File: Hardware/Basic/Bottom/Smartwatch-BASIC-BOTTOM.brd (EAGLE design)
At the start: 33 x 33 mm, 37 parts, among them U1 AD5242-SO16, U3 PCF8523

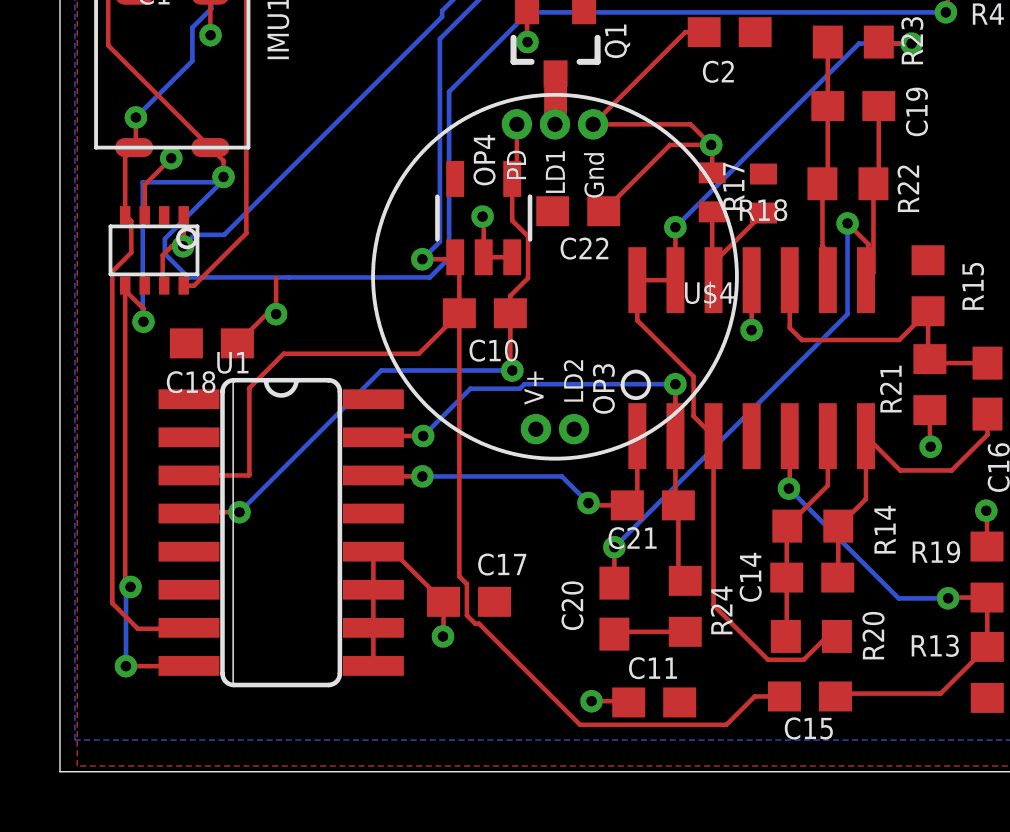
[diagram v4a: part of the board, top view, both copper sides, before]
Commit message: Bottom Board Complete
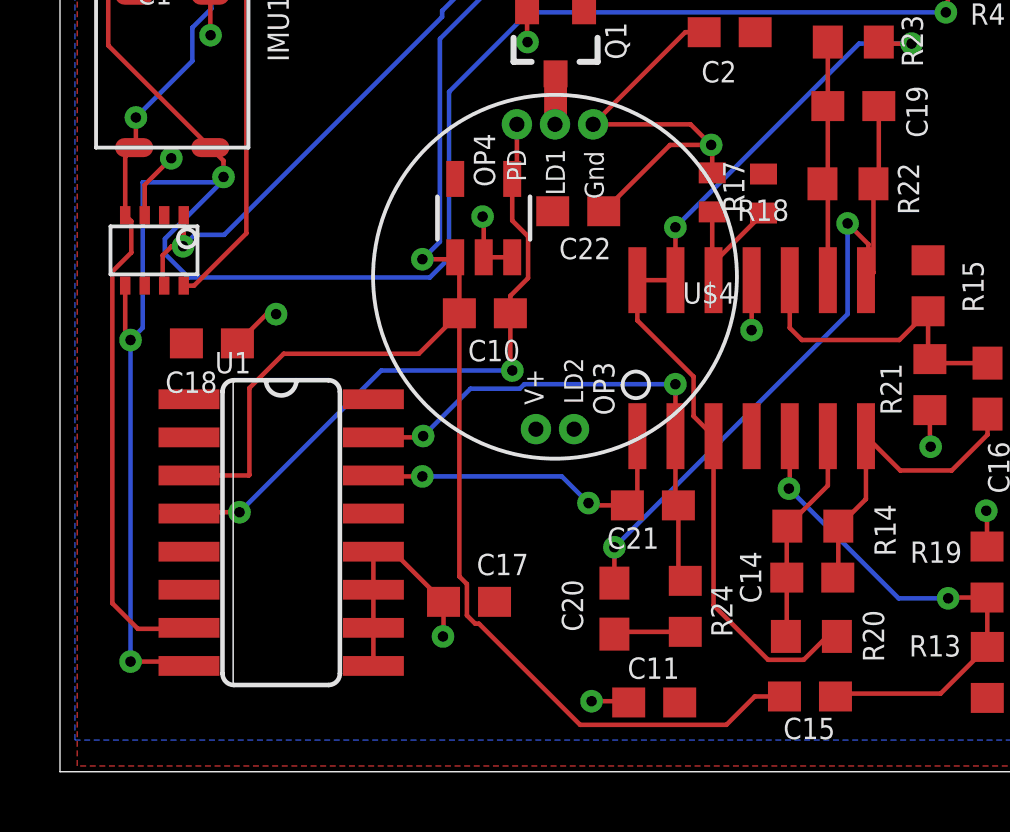
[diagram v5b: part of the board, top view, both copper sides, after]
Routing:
- net GND: track 40.9 -> 39.7 mm
- net SDA: track 76.0 -> 75.0 mm, vias 5 -> 4
- net N$18: track 7.10 -> 8.08 mm
- net G.W2: track 16.7 -> 17.6 mm
- net SCL: track 56.6 -> 57.5 mm
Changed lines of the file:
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@@
 <wire x1="9.3882" y1="17.7546" x2="9.7028" y2="17.7546" width="0.1524" layer="1"/>
 <via x="9.7028" y="17.7546" extent="1-16" drill="0.35"/>
-<wire x1="9.7028" y1="18.962" x2="9.7028" y2="17.7546" width="0.1524" layer="1"/>
 <wire x1="9.7536" y1="17.7038" x2="9.7028" y2="17.7546" width="0.1524" layer="1"/>
 </signal>
@@
 <wire x1="5.4614" y1="29.8034" x2="5.4614" y2="28.8744" width="0.1524" layer="1"/>
 <wire x1="5.4614" y1="28.8744" x2="4.9718" y2="28.3848" width="0.1524" layer="1"/>
-<wire x1="5.3238" y1="18.7024" x2="6.7136" y2="16.78" width="0" layer="19" extent="1-1"/>
 </signal>
 <signal name="SDA">
@@
 <wire x1="31.9096" y1="29.3368" x2="32.0936" y2="29.1528" width="0.1524" layer="1"/>
 <contactref element="J1" pad="1"/>
-<wire x1="4.6738" y1="18.7024" x2="4.6738" y2="8.8392" width="0.1524" layer="1"/>
-<wire x1="4.6738" y1="8.8392" x2="4.8516" y2="8.6614" width="0.1524" layer="1"/>
-<via x="4.8516" y="8.6614" extent="1-16" drill="0.35"/>
-<wire x1="4.8516" y1="8.6614" x2="4.699" y2="8.5088" width="0.1524" layer="16"/>
-<wire x1="4.699" y1="8.5088" x2="4.699" y2="6.0198" width="0.1524" layer="16"/>
-<via x="4.699" y="6.0198" extent="1-16" drill="0.35"/>
-<wire x1="4.699" y1="6.0198" x2="6.793" y2="6.0198" width="0.1524" layer="1"/>
 <wire x1="6.793" y1="6.0198" x2="6.7996" y2="6.0264" width="0.1524" layer="1"/>
 <wire x1="5" y1="33" x2="5" y2="30.7152875" width="0.1524" layer="1"/>
@@
 <wire x1="7.9502" y1="22.3266" x2="7.7724" y2="22.1488" width="0.1524" layer="16"/>
 <wire x1="7.7724" y1="22.1488" x2="5.2578" y2="22.1488" width="0.1524" layer="16"/>
-<wire x1="5.2578" y1="22.1488" x2="5.2578" y2="17.526" width="0.1524" layer="16"/>
-<wire x1="5.2578" y1="17.526" x2="5.2832" y2="17.5006" width="0.1524" layer="16"/>
-<via x="5.2832" y="17.5006" extent="1-16" drill="0.35"/>
-<wire x1="5.2832" y1="17.5006" x2="5.2832" y2="17.9324" width="0.1524" layer="1"/>
-<wire x1="5.2832" y1="17.9447125" x2="5.2832" y2="17.9324" width="0.1524" layer="1"/>
 <wire x1="32.0936" y1="29.1528" x2="32.0936" y2="27.8772" width="0.1524" layer="1"/>
 <wire x1="32.0936" y1="27.8772" x2="32.0294" y2="27.813" width="0.1524" layer="1"/>
@@
 <wire x1="5.9972" y1="20.26655" x2="7.9502" y2="22.21955" width="0.1524" layer="16"/>
 <wire x1="7.9502" y1="22.21955" x2="7.9502" y2="22.3266" width="0.1524" layer="16"/>
-<wire x1="14.83095" y1="18.9766" x2="10.1346" y2="18.9766" width="0.1524" layer="16"/>
-<wire x1="10.1346" y1="18.9766" x2="6.78445" y2="18.9766" width="0.1524" layer="16"/>
+<wire x1="14.83095" y1="18.9766" x2="6.78445" y2="18.9766" width="0.1524" layer="16"/>
 <wire x1="6.78445" y1="18.9766" x2="5.9972" y2="19.76385" width="0.1524" layer="16"/>
 <wire x1="7.5118" y1="23.3048" x2="7.9502" y2="22.8664" width="0.1524" layer="1"/>
 <wire x1="7.9502" y1="22.8664" x2="7.9502" y2="22.3266" width="0.1524" layer="1"/>
-<wire x1="5.2832" y1="17.9324" x2="4.6738" y2="18.5418" width="0.1524" layer="1"/>
-<wire x1="4.6738" y1="18.5418" x2="4.6738" y2="18.7024" width="0.1524" layer="1"/>
+<wire x1="4.6738" y1="17.0688" x2="4.8516" y2="16.891" width="0.1524" layer="1"/>
+<via x="4.8516" y="16.891" extent="1-16" drill="0.35"/>
+<wire x1="5.2578" y1="17.2972" x2="4.8516" y2="16.891" width="0.1524" layer="16"/>
+<wire x1="5.2578" y1="22.1488" x2="5.2578" y2="17.2972" width="0.1524" layer="16"/>
+<wire x1="4.8516" y1="16.891" x2="4.8516" y2="6.1724" width="0.1524" layer="16"/>
+<via x="4.8516" y="6.1724" extent="1-16" drill="0.35"/>
+<wire x1="4.8516" y1="6.1724" x2="6.6404" y2="6.1724" width="0.1524" layer="1"/>
+<wire x1="6.6404" y1="6.1724" x2="6.793" y2="6.0198" width="0.1524" layer="1"/>
+<wire x1="4.6738" y1="18.7024" x2="4.6738" y2="17.0688" width="0.1524" layer="1"/>
 </signal>
 <signal name="SCL">
@@
 <contactref element="J1" pad="2"/>
 <wire x1="4.2448" y1="8.1168875" x2="5.0972875" y2="7.2644" width="0.1524" layer="1"/>
-<wire x1="5.0972875" y1="7.2644" x2="5.969" y2="7.2644" width="0.1524" layer="1"/>
 <wire x1="7.54" y1="33" x2="7.54" y2="31.068" width="0.1524" layer="1"/>
 <wire x1="7.54" y1="31.068" x2="7.5438" y2="31.0642" width="0.1524" layer="1"/>
@@
 <wire x1="32.3088" y1="32.0548" x2="31.8996" y2="31.6456" width="0.1524" layer="16"/>
 <wire x1="31.8996" y1="31.6456" x2="14.91245" y2="31.6456" width="0.1524" layer="16"/>
-<wire x1="5.969" y1="7.2644" x2="6.7996" y2="7.2964" width="0" layer="19" extent="1-1"/>
+<wire x1="5.0972875" y1="7.2644" x2="6.7676" y2="7.2644" width="0.1524" layer="1"/>
+<wire x1="6.7676" y1="7.2644" x2="6.7996" y2="7.2964" width="0.1524" layer="1"/>
 </signal>
 <signal name="A6/TIA">
@@
 <wire x1="16.1826" y1="15.2682" x2="14.605" y2="13.6906" width="0.1524" layer="16"/>
 <wire x1="17.82815" y1="15.2682" x2="16.1826" y2="15.2682" width="0.1524" layer="16"/>
-<wire x1="14.605" y1="13.6906" x2="13.7922" y2="13.6906" width="0.1524" layer="1"/>
 <wire x1="13.7922" y1="13.6906" x2="13.7414" y2="13.6398" width="0.1524" layer="1"/>
-<wire x1="13.7414" y1="13.6398" x2="12.9464" y2="13.6464" width="0" layer="19" extent="1-1"/>
+<wire x1="14.605" y1="13.6906" x2="14.5608" y2="13.6464" width="0.1524" layer="1"/>
+<wire x1="14.5608" y1="13.6464" x2="12.9464" y2="13.6464" width="0.1524" layer="1"/>
+<wire x1="14.605" y1="13.6906" x2="13.7922" y2="13.6906" width="0" layer="19" extent="1-1"/>
 </signal>
 <signal name="G.A1">
@@
 <contactref element="C19" pad="2"/>
 <contactref element="R23" pad="2"/>
-<wire x1="27.9152" y1="22.098" x2="27.9152" y2="20.0146" width="0.1524" layer="1"/>
-<wire x1="27.9152" y1="20.0146" x2="28.067" y2="19.8628" width="0.1524" layer="1"/>
 <wire x1="28.093" y1="24.6888" x2="28.093" y2="22.2758" width="0.1524" layer="1"/>
 <wire x1="28.093" y1="22.2758" x2="27.9152" y2="22.098" width="0.1524" layer="1"/>
 <wire x1="28.0936" y1="26.8224" x2="28.0936" y2="24.6894" width="0.1524" layer="1"/>
 <wire x1="28.0936" y1="24.6894" x2="28.093" y2="24.6888" width="0.1524" layer="1"/>
-<wire x1="28.067" y1="19.8628" x2="28.0952" y2="18.886" width="0" layer="19" extent="1-1"/>
+<wire x1="27.9152" y1="22.098" x2="28.0952" y2="21.918" width="0.1524" layer="1"/>
+<wire x1="28.0952" y1="21.918" x2="28.0952" y2="18.886" width="0.1524" layer="1"/>
 </signal>
 <signal name="N$19">

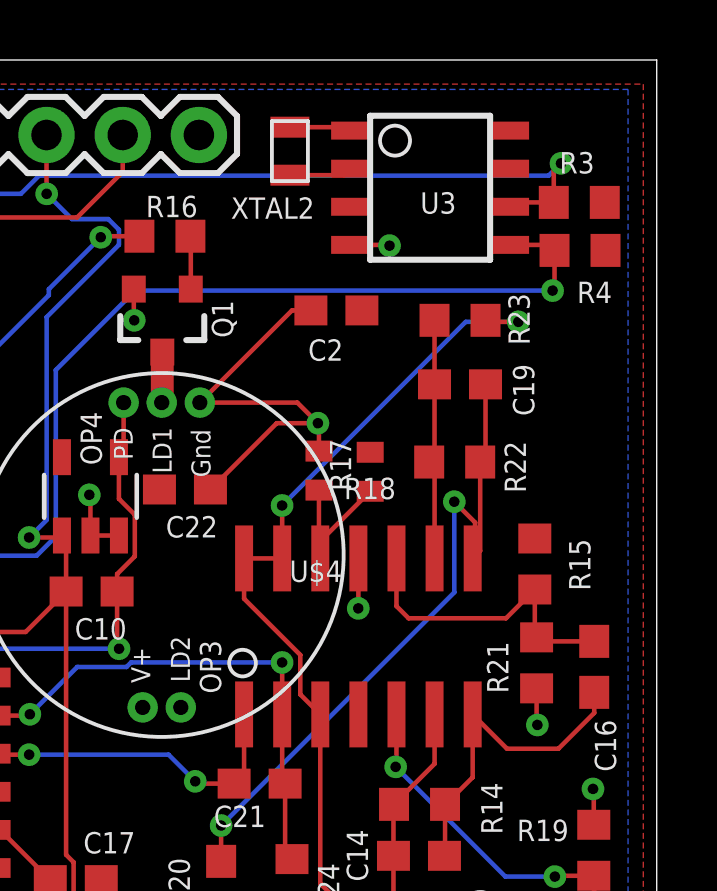
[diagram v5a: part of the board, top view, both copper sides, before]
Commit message: Organized Schematics and Silkscreens for both boards
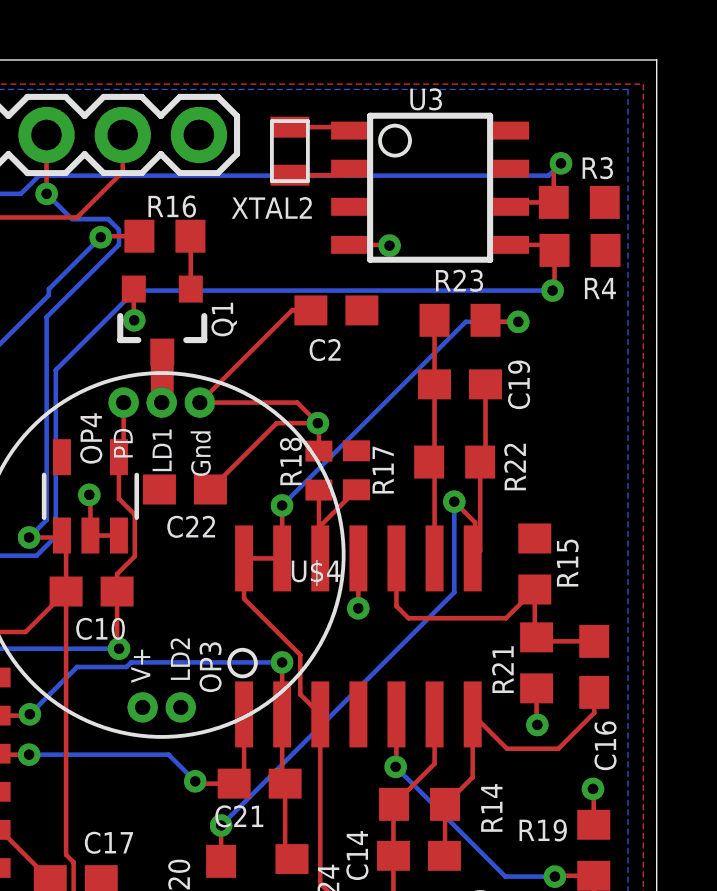
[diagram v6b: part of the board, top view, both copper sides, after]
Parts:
- moved R17 0.46 mm to (25.5, 21.8)
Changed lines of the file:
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@@
 <drawing>
 <settings>
-<setting alwaysvectorfont="no"/>
+<setting alwaysvectorfont="yes"/>
 <setting verticaltext="up"/>
 </settings>
@@
 </element>
 <element name="R15" library="LinnesLab-Passives" package="R0603" package3d_urn="urn:adsk.eagle:package:15661944/2" value="220k" x="31.4358" y="18.7" smashed="yes" rot="R90" grouprefs="PPG">
-<attribute name="NAME" x="33.29" y="17.811" size="0.7112" layer="25" rot="R90"/>
+<attribute name="NAME" x="32.8836" y="17.8618" size="0.7112" layer="25" rot="R90"/>
 <attribute name="VALUE" x="33.3408" y="18.065" size="1.27" layer="27" rot="R90"/>
 </element>
@@
 <attribute name="VALUE" x="31.3972" y="14.381" size="1.27" layer="27" rot="R90"/>
 </element>
-<element name="R17" library="LinnesLab-Passives" package="R0402" package3d_urn="urn:adsk.eagle:package:15661898/2" value="10k" x="25.9494" y="21.7734" smashed="yes" rot="R90" grouprefs="PPG">
-<attribute name="NAME" x="25.3144" y="21.1384" size="0.7112" layer="25" rot="R90"/>
-<attribute name="VALUE" x="27.8544" y="21.1384" size="1.27" layer="27" rot="R90"/>
+<element name="R17" library="LinnesLab-Passives" package="R0402" package3d_urn="urn:adsk.eagle:package:15661898/2" value="10k" x="25.4922" y="21.8242" smashed="yes" rot="R90" grouprefs="PPG">
+<attribute name="NAME" x="26.7368" y="20.9606" size="0.7112" layer="25" rot="R90"/>
+<attribute name="VALUE" x="27.3972" y="21.1892" size="1.27" layer="27" rot="R90"/>
 </element>
 <element name="R18" library="LinnesLab-Passives" package="R0402" package3d_urn="urn:adsk.eagle:package:15661898/2" value="10k" x="24.241" y="21.813" smashed="yes" rot="R270" grouprefs="PPG">
-<attribute name="NAME" x="25.0754" y="20.8628" size="0.7112" layer="25"/>
+<attribute name="NAME" x="23.6634" y="21.24" size="0.7112" layer="25" rot="R90"/>
 <attribute name="VALUE" x="22.336" y="22.448" size="1.27" layer="27" rot="R270"/>
 </element>
@@
 </element>
 <element name="R21" library="LinnesLab-Passives" package="R0603" package3d_urn="urn:adsk.eagle:package:15661944/2" value="220k" x="31.496" y="15.4048" smashed="yes" rot="R90" grouprefs="PPG">
-<attribute name="NAME" x="29.845" y="16.1166" size="0.7112" layer="25" rot="R270"/>
+<attribute name="NAME" x="30.0228" y="16.0404" size="0.7112" layer="25" rot="R270"/>
 <attribute name="VALUE" x="33.401" y="16.7698" size="1.27" layer="27" rot="R90"/>
 </element>
@@
 </element>
 <element name="C19" library="LinnesLab-Passives" package="C0603" package3d_urn="urn:adsk.eagle:package:15661989/2" value="2.2n" x="28.943" y="24.6888" smashed="yes" rot="R180" grouprefs="PPG">
-<attribute name="NAME" x="31.4198" y="23.635" size="0.7112" layer="25" rot="R90"/>
+<attribute name="NAME" x="31.2674" y="23.8128" size="0.7112" layer="25" rot="R90"/>
 <attribute name="VALUE" x="29.578" y="26.5938" size="1.27" layer="27" rot="R180"/>
 </element>
 <element name="R23" library="LinnesLab-Passives" package="R0603" package3d_urn="urn:adsk.eagle:package:15661944/2" value="1M" x="28.9436" y="26.8224" smashed="yes" rot="R180" grouprefs="PPG">
-<attribute name="NAME" x="31.2674" y="25.9966" size="0.7112" layer="25" rot="R90"/>
+<attribute name="NAME" x="29.7818" y="28.4988" size="0.7112" layer="25" rot="R180"/>
 <attribute name="VALUE" x="29.5786" y="28.7274" size="1.27" layer="27" rot="R180"/>
 </element>
@@
 </element>
 <element name="R3" library="LinnesLab-Passives" package="R0603" package3d_urn="urn:adsk.eagle:package:15661944/2" value="10k" x="32.9182" y="30.753" smashed="yes" grouprefs="RTC">
-<attribute name="NAME" x="32.2578" y="31.7182" size="0.7112" layer="25"/>
+<attribute name="NAME" x="32.9436" y="31.5404" size="0.7112" layer="25"/>
 <attribute name="VALUE" x="32.2832" y="28.848" size="0.7112" layer="27"/>
 </element>
 <element name="R4" library="LinnesLab-Passives" package="R0603" package3d_urn="urn:adsk.eagle:package:15661944/2" value="10k" x="32.9436" y="29.1528" smashed="yes" grouprefs="RTC">
-<attribute name="NAME" x="32.842" y="27.4002" size="0.7112" layer="25"/>
+<attribute name="NAME" x="33.0198" y="27.5272" size="0.7112" layer="25"/>
 <attribute name="VALUE" x="32.3086" y="27.2478" size="0.7112" layer="27"/>
 </element>
@@
 <attribute name="MFN" value="PCF8523T/1,118" x="27.9464" y="31.2418" size="1.778" layer="27" display="off"/>
 <attribute name="MFN_MANUFACTURER" value="NXP USA Inc." x="27.9464" y="31.2418" size="1.778" layer="27" display="off"/>
-<attribute name="NAME" x="27.6162" y="30.3782" size="0.7112" layer="25"/>
+<attribute name="NAME" x="27.2098" y="33.8326" size="0.7112" layer="25"/>
 <attribute name="VALUE" x="26.0414" y="27.6858" size="0.7112" layer="27"/>
 </element>
@@
 <wire x1="24.2852" y1="18.886" x2="24.241" y2="18.9302" width="0.1524" layer="1"/>
 <wire x1="24.241" y1="18.9302" x2="24.241" y2="21.163" width="0.1524" layer="1"/>
-<wire x1="24.2852" y1="18.886" x2="24.2852" y2="19.4592" width="0.1524" layer="1"/>
-<wire x1="24.2852" y1="19.4592" x2="25.9494" y2="21.1234" width="0.1524" layer="1"/>
+<wire x1="24.2852" y1="18.886" x2="24.2852" y2="19.9672" width="0.1524" layer="1"/>
+<wire x1="24.2852" y1="19.9672" x2="25.4922" y2="21.1742" width="0.1524" layer="1"/>
 </signal>
 <signal name="G.W2">

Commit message: Fixed Bottom Board Issue
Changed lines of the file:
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@@
 <drawing>
 <settings>
-<setting alwaysvectorfont="yes"/>
+<setting alwaysvectorfont="no"/>
 <setting verticaltext="up"/>
 </settings>
@@
 <wire x1="26.5686" y1="29.3368" x2="26.5938" y2="29.3116" width="0.1524" layer="1"/>
 <via x="26.5938" y="29.3116" extent="1-16" drill="0.35"/>
-<wire x1="7.1614" y1="29.8034" x2="7.203" y2="29.845" width="0.1524" layer="1"/>
 <wire x1="7.5118" y1="28.3848" x2="7.5118" y2="27.0576" width="0.1524" layer="1"/>
 <wire x1="7.5184" y1="27.051" x2="7.5118" y2="27.0576" width="0.1524" layer="1"/>
@@
 <wire x1="9.3882" y1="17.7546" x2="9.7028" y2="17.7546" width="0.1524" layer="1"/>
 <via x="9.7028" y="17.7546" extent="1-16" drill="0.35"/>
-<wire x1="9.7536" y1="17.7038" x2="9.7028" y2="17.7546" width="0.1524" layer="1"/>
 </signal>
 <signal name="3.3V">
@@
 <wire x1="23.0152" y1="15.415" x2="23.0124" y2="15.4178" width="0.1524" layer="1"/>
 <via x="23.0124" y="15.4178" extent="1-16" drill="0.35"/>
-<via x="14.605" y="13.6906" extent="1-16" drill="0.35"/>
 <wire x1="23.0124" y1="15.4178" x2="17.97775" y2="15.4178" width="0.1524" layer="16"/>
 <wire x1="17.97775" y1="15.4178" x2="17.82815" y2="15.2682" width="0.1524" layer="16"/>
 <wire x1="16.1826" y1="15.2682" x2="14.605" y2="13.6906" width="0.1524" layer="16"/>
 <wire x1="17.82815" y1="15.2682" x2="16.1826" y2="15.2682" width="0.1524" layer="16"/>
-<wire x1="13.7922" y1="13.6906" x2="13.7414" y2="13.6398" width="0.1524" layer="1"/>
+<via x="14.605" y="13.6906" extent="1-16" drill="0.35"/>
 <wire x1="14.605" y1="13.6906" x2="14.5608" y2="13.6464" width="0.1524" layer="1"/>
 <wire x1="14.5608" y1="13.6464" x2="12.9464" y2="13.6464" width="0.1524" layer="1"/>
-<wire x1="14.605" y1="13.6906" x2="13.7922" y2="13.6906" width="0" layer="19" extent="1-1"/>
 </signal>
 <signal name="G.A1">
